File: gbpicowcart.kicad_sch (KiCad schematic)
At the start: 15 parts, among them J1 Conn_01x03, J2 GameBoy_Cartridge, J3 Conn_01x11_Female, U1 PicoW, U2 TXS0108EPW, U3 TXS0108EPW, U4 TXS0108EPW, U5 TXS0108EPW, U6 74AHC1G00

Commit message: wip
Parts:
- removed D1, D2: 1N4001, Diode_THT:D_DO-41_SOD81_P10.16mm_Horizontal, symbol Diode:1N4001
- added D? (x2): D_Schottky, symbol Device:D_Schottky
- J1: footprint (none) -> Connector_PinHeader_2.54mm:PinHeader_1x03_P2.54mm_Vertical
- J2: footprint (none) -> Gekkio_Connector_PCBEdge:GameBoy_Cartridge_1x32_P1.50mm_Edge
- J3: footprint (none) -> Connector_PinHeader_2.54mm:PinHeader_1x11_P2.54mm_Vertical
- JP1, JP2: footprint (none) -> Jumper:SolderJumper-2_P1.3mm_Open_Pad1.0x1.5mm
- R1: footprint (none) -> Resistor_SMD:R_0805_2012Metric; LCSC (none) -> C350556
- R2: footprint (none) -> Resistor_SMD:R_0805_2012Metric
- U2: LCSC (none) -> C17206
- U6: footprint (none) -> Package_TO_SOT_SMD:SOT-23-5
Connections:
- net VCC: now also D?.1 (K), D?.2 (A)
- net at J2.1 (VCC): now also D?.2 (A)
- net at U1.39 (VSYS): now also D?.1 (K)
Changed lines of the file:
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@@
     )
-  )
-  (symbol (lib_id "Diode:1N4001") (at 248.031 46.355 0) (unit 1)
-    (in_bom yes) (on_board yes) (fields_autoplaced)
-    (property "Reference" "D1" (id 0) (at 248.031 39.37 0))
-    (property "Value" "1N4001" (id 1) (at 248.031 41.91 0))
-    (property "Footprint" "Diode_THT:D_DO-41_SOD81_P10.16mm_Horizontal" (id 2) (at 248.031 50.8 0)
-      (effects (font (size 1.27 1.27)) hide)
-    )
-    (property "Datasheet" "http://www.vishay.com/docs/88503/1n4001.pdf" (id 3) (at 248.031 46.355 0)
-      (effects (font (size 1.27 1.27)) hide)
-    )
-    (pin "1")
-    (pin "2")
   )
   (symbol (lib_id "Logic_LevelTranslator:TXS0108EPW") (at 198.501 43.053 0) (unit 1)
@@
       (effects (font (size 1.27 1.27)) hide)
     )
+    (property "LCSC" "C17206" (id 4) (at 140.716 96.393 0)
+      (effects (font (size 1.27 1.27)) hide)
+    )
     (pin "1")
     (pin "10")
@@
     (property "Reference" "JP1" (id 0) (at 107.823 174.244 0))
     (property "Value" "Jumper_2_Bridged" (id 1) (at 107.823 176.784 0))
-    (property "Footprint" "" (id 2) (at 107.823 179.578 0)
+    (property "Footprint" "Jumper:SolderJumper-2_P1.3mm_Open_Pad1.0x1.5mm" (id 2) (at 107.823 179.578 0)
       (effects (font (size 1.27 1.27)) hide)
     )
@@
     (pin "9")
   )
+  (symbol (lib_id "Device:D_Schottky") (at 248.031 46.355 0) (unit 1)
+    (in_bom yes) (on_board yes) (fields_autoplaced)
+    (property "Reference" "D?" (id 0) (at 247.7135 39.497 0))
+    (property "Value" "D_Schottky" (id 1) (at 247.7135 42.037 0))
+    (property "Footprint" "" (id 2) (at 248.031 46.355 0)
+      (effects (font (size 1.27 1.27)) hide)
+    )
+    (property "Datasheet" "~" (id 3) (at 248.031 46.355 0)
+      (effects (font (size 1.27 1.27)) hide)
+    )
+    (pin "1")
+    (pin "2")
+  )
   (symbol (lib_id "power:GND") (at 190.627 62.865 270) (unit 1)
     (in_bom yes) (on_board yes) (fields_autoplaced)
@@
     (property "Reference" "JP2" (id 0) (at 107.95 164.211 0))
     (property "Value" "Jumper_2_Bridged" (id 1) (at 107.95 166.751 0))
-    (property "Footprint" "" (id 2) (at 107.95 169.545 0)
+    (property "Footprint" "Jumper:SolderJumper-2_P1.3mm_Open_Pad1.0x1.5mm" (id 2) (at 107.95 169.545 0)
       (effects (font (size 1.27 1.27)) hide)
     )
@@
     (property "Reference" "R1" (id 0) (at 144.272 175.26 90))
     (property "Value" "1K ohm" (id 1) (at 144.272 172.72 90))
-    (property "Footprint" "" (id 2) (at 144.272 167.767 90)
+    (property "Footprint" "Resistor_SMD:R_0805_2012Metric" (id 2) (at 144.272 167.767 90)
       (effects (font (size 1.27 1.27)) hide)
     )
@@
       (effects (font (size 1.27 1.27)) hide)
     )
+    (property "LCSC" "C350556" (id 4) (at 144.272 169.545 90)
+      (effects (font (size 1.27 1.27)) hide)
+    )
     (pin "1")
     (pin "2")
@@
       (effects (font (size 1.27 1.27)) (justify left))
     )
-    (property "Footprint" "" (id 2) (at 56.642 95.631 0)
+    (property "Footprint" "Connector_PinHeader_2.54mm:PinHeader_1x03_P2.54mm_Vertical" (id 2) (at 56.642 95.631 0)
       (effects (font (size 1.27 1.27)) hide)
     )
@@
       (effects (font (size 1.27 1.27)) (justify left))
     )
-    (property "Footprint" "" (id 2) (at 259.461 132.715 0)
+    (property "Footprint" "Gekkio_Connector_PCBEdge:GameBoy_Cartridge_1x32_P1.50mm_Edge" (id 2) (at 259.461 132.715 0)
       (effects (font (size 1.27 1.27)) hide)
     )
@@
     (property "Reference" "U6" (id 0) (at 42.799 161.417 0))
     (property "Value" "74AHC1G00" (id 1) (at 42.799 163.957 0))
-    (property "Footprint" "" (id 2) (at 43.434 169.291 0)
+    (property "Footprint" "Package_TO_SOT_SMD:SOT-23-5" (id 2) (at 43.434 169.291 0)
       (effects (font (size 1.27 1.27)) hide)
     )
@@
     (pin "4")
     (pin "5")
+  )
+  (symbol (lib_id "Device:D_Schottky") (at 83.566 33.401 0) (unit 1)
+    (in_bom yes) (on_board yes) (fields_autoplaced)
+    (property "Reference" "D?" (id 0) (at 83.2485 26.543 0))
+    (property "Value" "D_Schottky" (id 1) (at 83.2485 29.083 0))
+    (property "Footprint" "" (id 2) (at 83.566 33.401 0)
+      (effects (font (size 1.27 1.27)) hide)
+    )
+    (property "Datasheet" "~" (id 3) (at 83.566 33.401 0)
+      (effects (font (size 1.27 1.27)) hide)
+    )
+    (pin "1")
+    (pin "2")
   )
   (symbol (lib_id "Device:R") (at 127.254 169.545 90) (unit 1)
@@
     (property "Reference" "R2" (id 0) (at 127.254 163.83 90))
     (property "Value" "500 ohm" (id 1) (at 127.254 166.37 90))
-    (property "Footprint" "" (id 2) (at 127.254 171.323 90)
+    (property "Footprint" "Resistor_SMD:R_0805_2012Metric" (id 2) (at 127.254 171.323 90)
       (effects (font (size 1.27 1.27)) hide)
     )
     (property "Datasheet" "~" (id 3) (at 127.254 169.545 0)
-      (effects (font (size 1.27 1.27)) hide)
-    )
-    (pin "1")
-    (pin "2")
-  )
-  (symbol (lib_id "Diode:1N4001") (at 83.566 33.401 0) (unit 1)
-    (in_bom yes) (on_board yes) (fields_autoplaced)
-    (property "Reference" "D2" (id 0) (at 83.566 26.416 0))
-    (property "Value" "1N4001" (id 1) (at 83.566 28.956 0))
-    (property "Footprint" "Diode_THT:D_DO-41_SOD81_P10.16mm_Horizontal" (id 2) (at 83.566 37.846 0)
-      (effects (font (size 1.27 1.27)) hide)
-    )
-    (property "Datasheet" "http://www.vishay.com/docs/88503/1n4001.pdf" (id 3) (at 83.566 33.401 0)
       (effects (font (size 1.27 1.27)) hide)
     )
@@
       (effects (font (size 1.27 1.27)) (justify left))
     )
-    (property "Footprint" "" (id 2) (at 42.672 125.857 0)
+    (property "Footprint" "Connector_PinHeader_2.54mm:PinHeader_1x11_P2.54mm_Vertical" (id 2) (at 42.672 125.857 0)
       (effects (font (size 1.27 1.27)) hide)
     )
@@
       (reference "#PWR0105") (unit 1) (value "GND") (footprint "")
     )
-    (path "/0061db95-6bf1-4f4a-b56d-75503749d6c8"
-      (reference "D1") (unit 1) (value "1N4001") (footprint "Diode_THT:D_DO-41_SOD81_P10.16mm_Horizontal")
-    )
-    (path "/f7297588-79a6-44cc-ba92-f71259f75959"
-      (reference "D2") (unit 1) (value "1N4001") (footprint "Diode_THT:D_DO-41_SOD81_P10.16mm_Horizontal")
+    (path "/22299e8c-847c-453f-971e-f5e8ac02082a"
+      (reference "D?") (unit 1) (value "D_Schottky") (footprint "")
+    )
+    (path "/e7d642ed-2a11-4dd2-9bb4-1cc071810cd6"
+      (reference "D?") (unit 1) (value "D_Schottky") (footprint "")
     )
     (path "/a41acfed-1e02-424b-8267-9a598336a6fe"
-      (reference "J1") (unit 1) (value "Conn_01x03") (footprint "")
+      (reference "J1") (unit 1) (value "Conn_01x03") (footprint "Connector_PinHeader_2.54mm:PinHeader_1x03_P2.54mm_Vertical")
     )
     (path "/aebb8237-1fa4-4151-998c-9d411c472ad3"
-      (reference "J2") (unit 1) (value "GameBoy_Cartridge") (footprint "")
+      (reference "J2") (unit 1) (value "GameBoy_Cartridge") (footprint "Gekkio_Connector_PCBEdge:GameBoy_Cartridge_1x32_P1.50mm_Edge")
     )
     (path "/f9d7b173-d2c4-4451-ad4c-b6785fe983bf"
-      (reference "J3") (unit 1) (value "Conn_01x11_Female") (footprint "")
+      (reference "J3") (unit 1) (value "Conn_01x11_Female") (footprint "Connector_PinHeader_2.54mm:PinHeader_1x11_P2.54mm_Vertical")
     )
     (path "/1634eef3-f89e-4239-ab82-4bf1d96af25d"
-      (reference "JP1") (unit 1) (value "Jumper_2_Bridged") (footprint "")
+      (reference "JP1") (unit 1) (value "Jumper_2_Bridged") (footprint "Jumper:SolderJumper-2_P1.3mm_Open_Pad1.0x1.5mm")
     )
     (path "/57336f44-2524-4efe-b897-718a2ae8d0e4"
-      (reference "JP2") (unit 1) (value "Jumper_2_Bridged") (footprint "")
+      (reference "JP2") (unit 1) (value "Jumper_2_Bridged") (footprint "Jumper:SolderJumper-2_P1.3mm_Open_Pad1.0x1.5mm")
     )
     (path "/a3278ef7-0788-46e5-8cc9-605d3adceb1f"
-      (reference "R1") (unit 1) (value "1K ohm") (footprint "")
+      (reference "R1") (unit 1) (value "1K ohm") (footprint "Resistor_SMD:R_0805_2012Metric")
     )
     (path "/f6b12c07-db25-4d68-8e72-3e0ced4fbbb5"
-      (reference "R2") (unit 1) (value "500 ohm") (footprint "")
+      (reference "R2") (unit 1) (value "500 ohm") (footprint "Resistor_SMD:R_0805_2012Metric")
     )
     (path "/ffcc49a4-4742-41bd-85d2-87452eb22aa1"
@@
     )
     (path "/d79b890f-d9b2-4d62-8d28-a0470b08a074"
-      (reference "U6") (unit 1) (value "74AHC1G00") (footprint "")
-    )
-  )
+      (reference "U6") (unit 1) (value "74AHC1G00") (footprint "Package_TO_SOT_SMD:SOT-23-5")
+    )
+  )

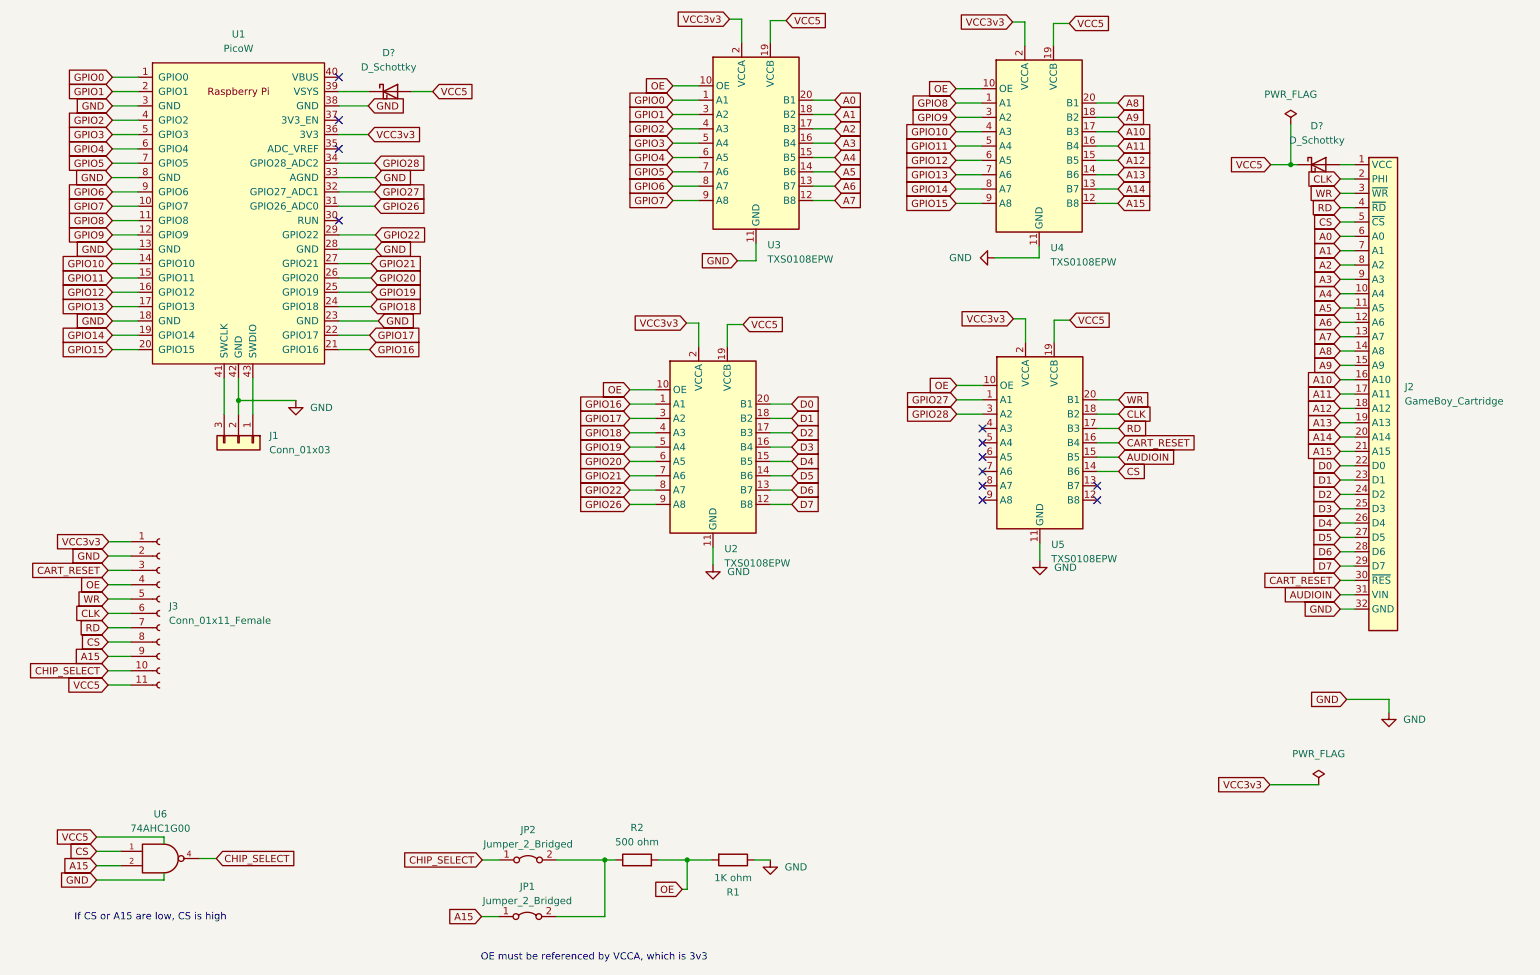
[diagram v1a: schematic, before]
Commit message: Remapped footprints for the first fabrication test
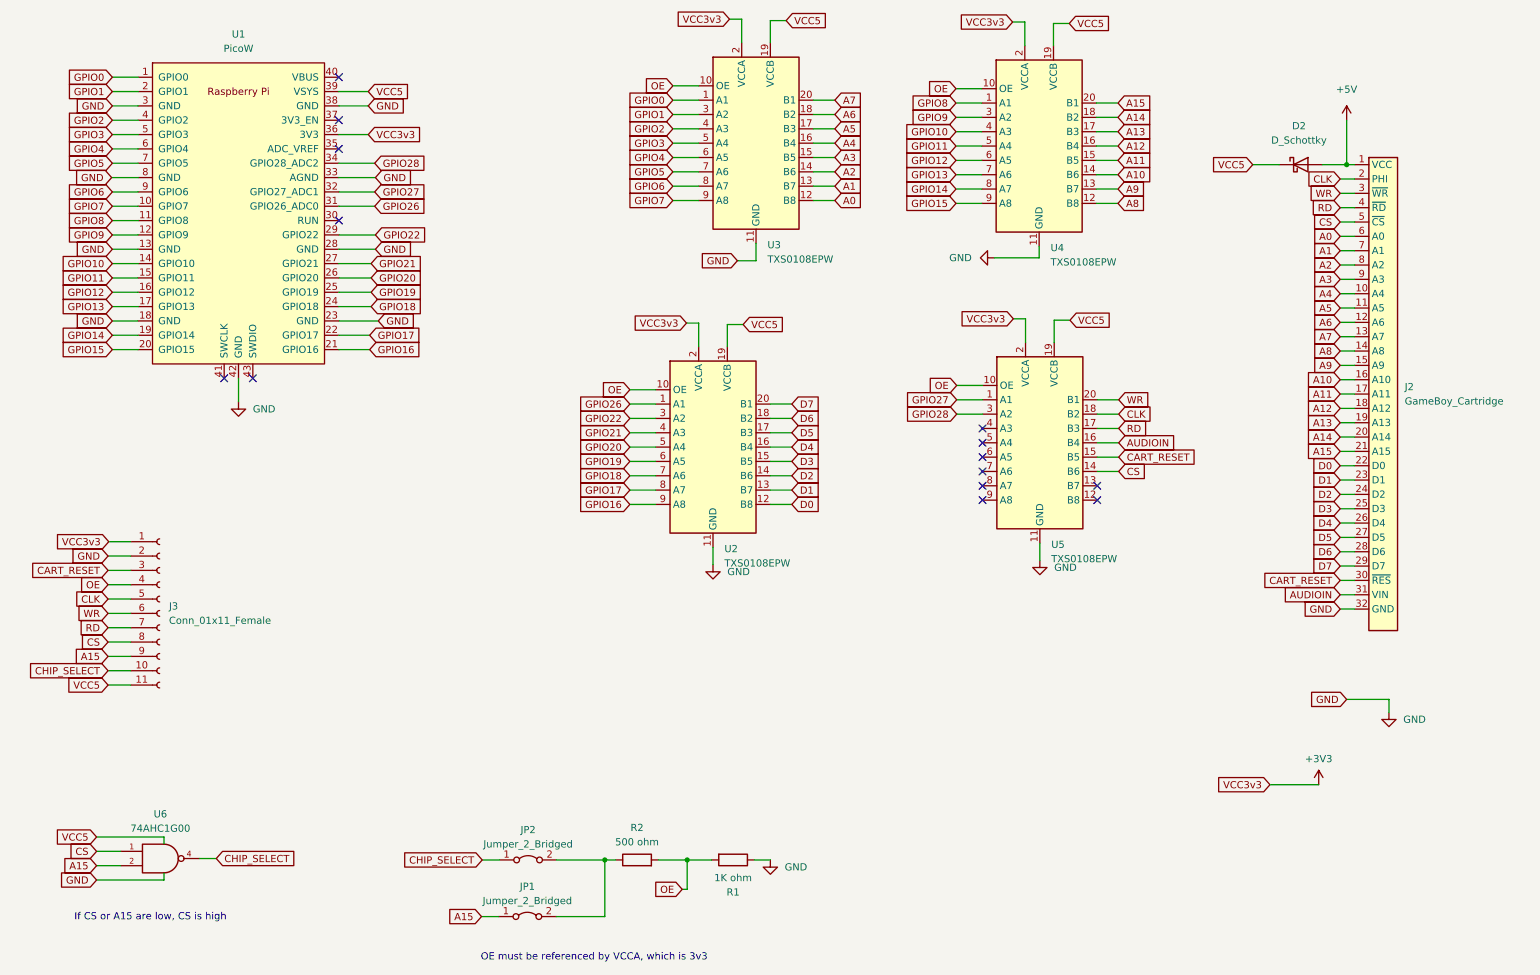
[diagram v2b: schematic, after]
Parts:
- removed D?: D_Schottky, symbol Device:D_Schottky
- removed J1: Conn_01x03, Connector_PinHeader_2.54mm:PinHeader_1x03_P2.54mm_Vertical, symbol Connector_Generic:Conn_01x03
- D2: renamed from D?; footprint (none) -> Diode_SMD:D_SOD-123; LCSC (none) -> C8598
- J2, J3, JP1, JP2: now left out of the parts list
- R1: LCSC C350556 -> C17513
- R2: LCSC (none) -> C17734
- U1: footprint RPi_PicoW:RPi_Pico_SMD_TH -> RPi_Pico:RPi_PicoW_SMD_TH; now left out of the parts list
- U3, U4, U5: LCSC (none) -> C17206
- U6: LCSC (none) -> C350556
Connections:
- net A0: now also U3.12 (B8); no longer U3.20 (B1)
- net A1: now also U3.13 (B7); no longer U3.18 (B2)
- net A10: now also U4.14 (B6); no longer U4.17 (B3)
- net A11: now also U4.15 (B5); no longer U4.16 (B4)
- net A12: now also U4.16 (B4); no longer U4.15 (B5)
- net A13: now also U4.17 (B3); no longer U4.14 (B6)
- net A14: now also U4.18 (B2); no longer U4.13 (B7)
- net A15: now also U4.20 (B1); no longer U4.12 (B8)
- net A2: now also U3.14 (B6); no longer U3.17 (B3)
- net A3: now also U3.15 (B5); no longer U3.16 (B4)
- net A4: now also U3.16 (B4); no longer U3.15 (B5)
- net A5: now also U3.17 (B3); no longer U3.14 (B6)
- net A6: now also U3.18 (B2); no longer U3.13 (B7)
- net A7: now also U3.20 (B1); no longer U3.12 (B8)
- net A8: now also U4.12 (B8); no longer U4.20 (B1)
- net A9: now also U4.13 (B7); no longer U4.18 (B2)
- net AUDIOIN: now also U5.16 (B4); no longer U5.15 (B5)
- net CART_RESET: now also U5.15 (B5); no longer U5.16 (B4)
- net CLK: now also J3.5 (Pin_5); no longer J3.6 (Pin_6)
- net D0: now also U2.12 (B8); no longer U2.20 (B1)
- net D1: now also U2.13 (B7); no longer U2.18 (B2)
- net D2: now also U2.14 (B6); no longer U2.17 (B3)
- net D3: now also U2.15 (B5); no longer U2.16 (B4)
- net D4: now also U2.16 (B4); no longer U2.15 (B5)
- net D5: now also U2.17 (B3); no longer U2.14 (B6)
- net D6: now also U2.18 (B2); no longer U2.13 (B7)
- net D7: now also U2.20 (B1); no longer U2.12 (B8)
- net GPIO16: now also U2.9 (A8); no longer U2.1 (A1)
- net GPIO17: now also U2.8 (A7); no longer U2.3 (A2)
- net GPIO18: now also U2.7 (A6); no longer U2.4 (A3)
- net GPIO19: now also U2.6 (A5); no longer U2.5 (A4)
- net GPIO20: now also U2.5 (A4); no longer U2.6 (A5)
- net GPIO21: now also U2.4 (A3); no longer U2.7 (A6)
- net GPIO22: now also U2.3 (A2); no longer U2.8 (A7)
- net GPIO26: now also U2.1 (A1); no longer U2.9 (A8)
- net VCC: now also U1.39 (VSYS)
- net WR: now also J3.6 (Pin_6); no longer J3.5 (Pin_5)
- net +5V: now reaches D2.2 (A), J2.1 (VCC)
- net VCC3v3 renamed +3V3
- no-connect marks 12 -> 14
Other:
- moved on the sheet: D2
